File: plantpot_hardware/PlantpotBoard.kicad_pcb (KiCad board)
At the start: 2 copper layers, 48.3 x 53.3 mm, 11 parts, among them J1 Solenoid, J2 Moisture Sensor, J3 Bus Connector, Q1 BD135-16, SW1 reset, U1 Pico

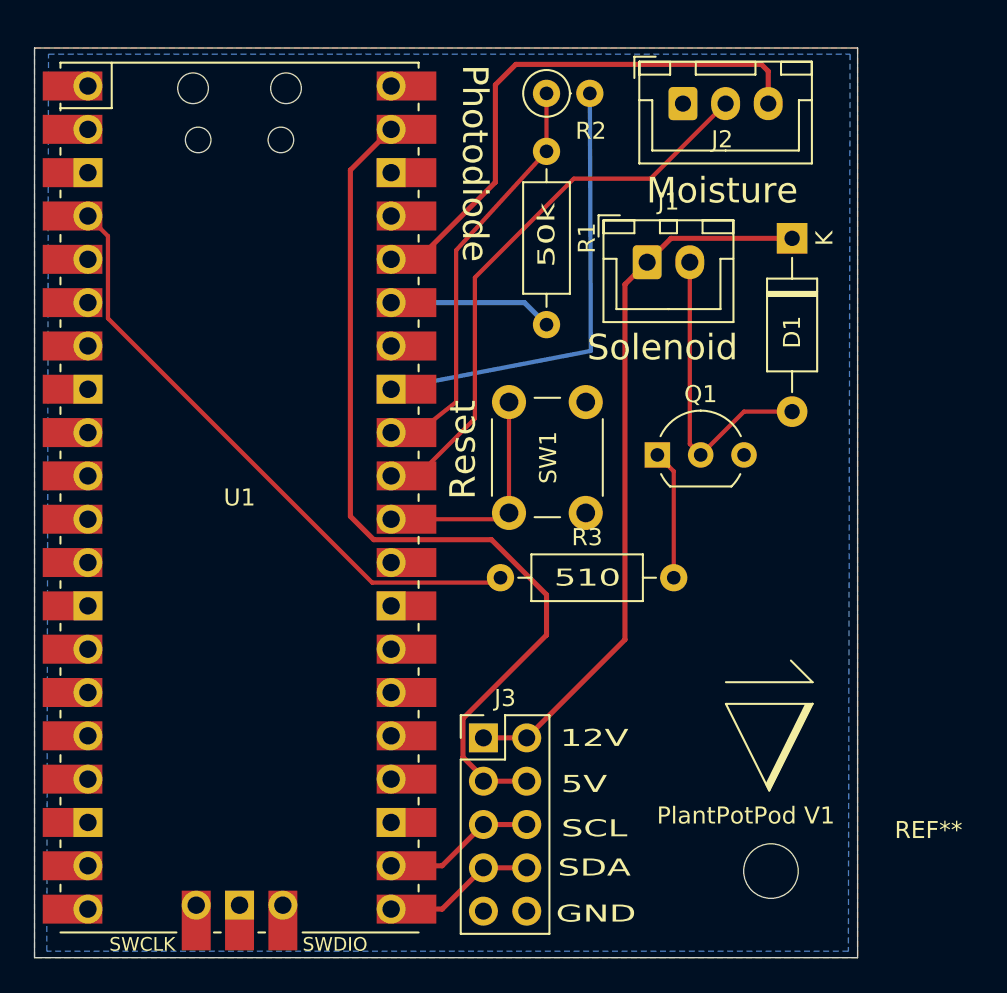
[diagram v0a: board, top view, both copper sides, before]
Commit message: added gerber files to the gitignore
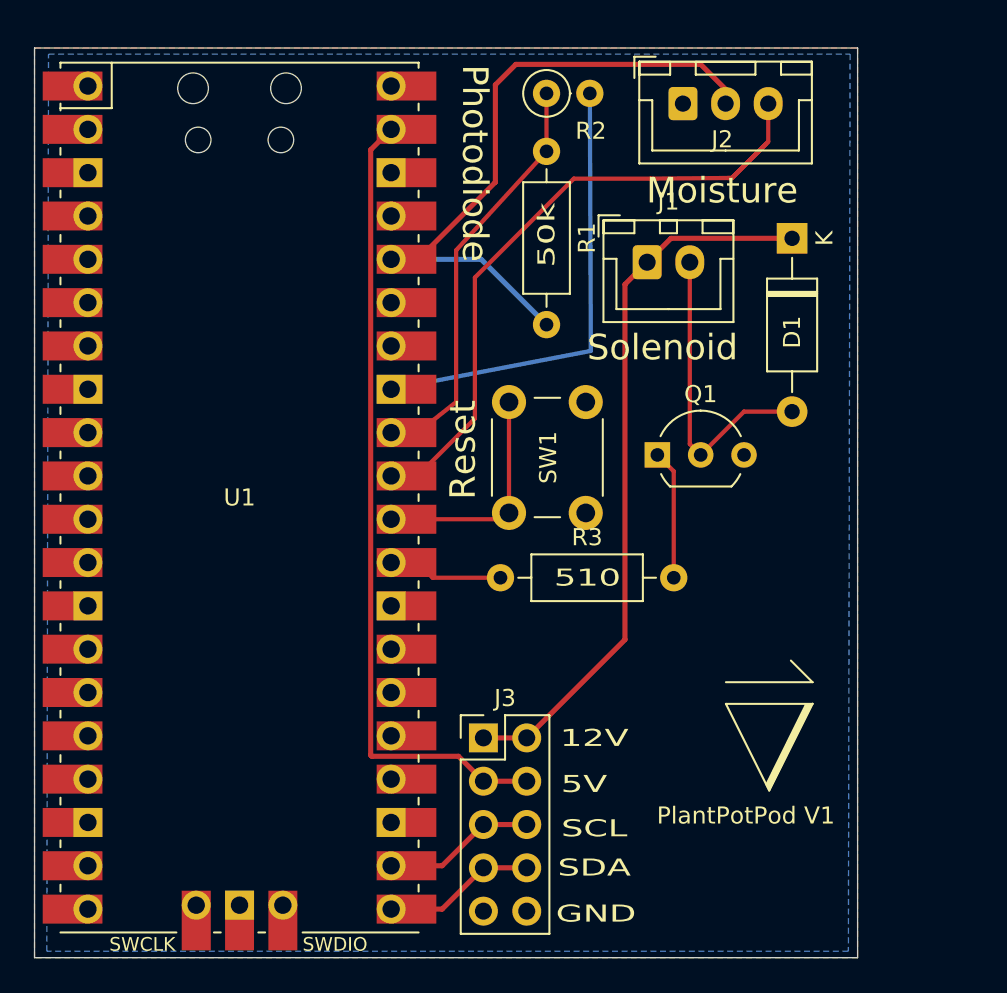
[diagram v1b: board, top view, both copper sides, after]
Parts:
- removed REF**: MountingHole_3.2mm_M3_DIN965, MountingHole:MountingHole_3.2mm_M3_DIN965
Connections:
- J2 pad 2: MOIST -> +3V3
- J2 pad 3: +3V3 -> MOIST
- R1 pad 2: +3.3VADC -> +3V3
- R3 pad 1: Net-(R3-Pad1) -> Solenoid
- U1 pad 29: Net-(U1-Pad29) -> Solenoid
- U1 pad 4: Net-(R3-Pad1) -> Net-(U1-Pad4)
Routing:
- net Net-(R3-Pad1): track 36.0 -> 0.00 mm
- net +3.3VADC: track 9.64 -> 0.00 mm
- net +3V3: track 32.3 -> 39.8 mm
- net Solenoid: track 0.00 -> 7.18 mm
- net MOIST: track 33.5 -> 40.4 mm
- net +5V: track 53.4 -> 47.0 mm
